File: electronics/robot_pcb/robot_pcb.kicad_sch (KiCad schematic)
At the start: 6 parts

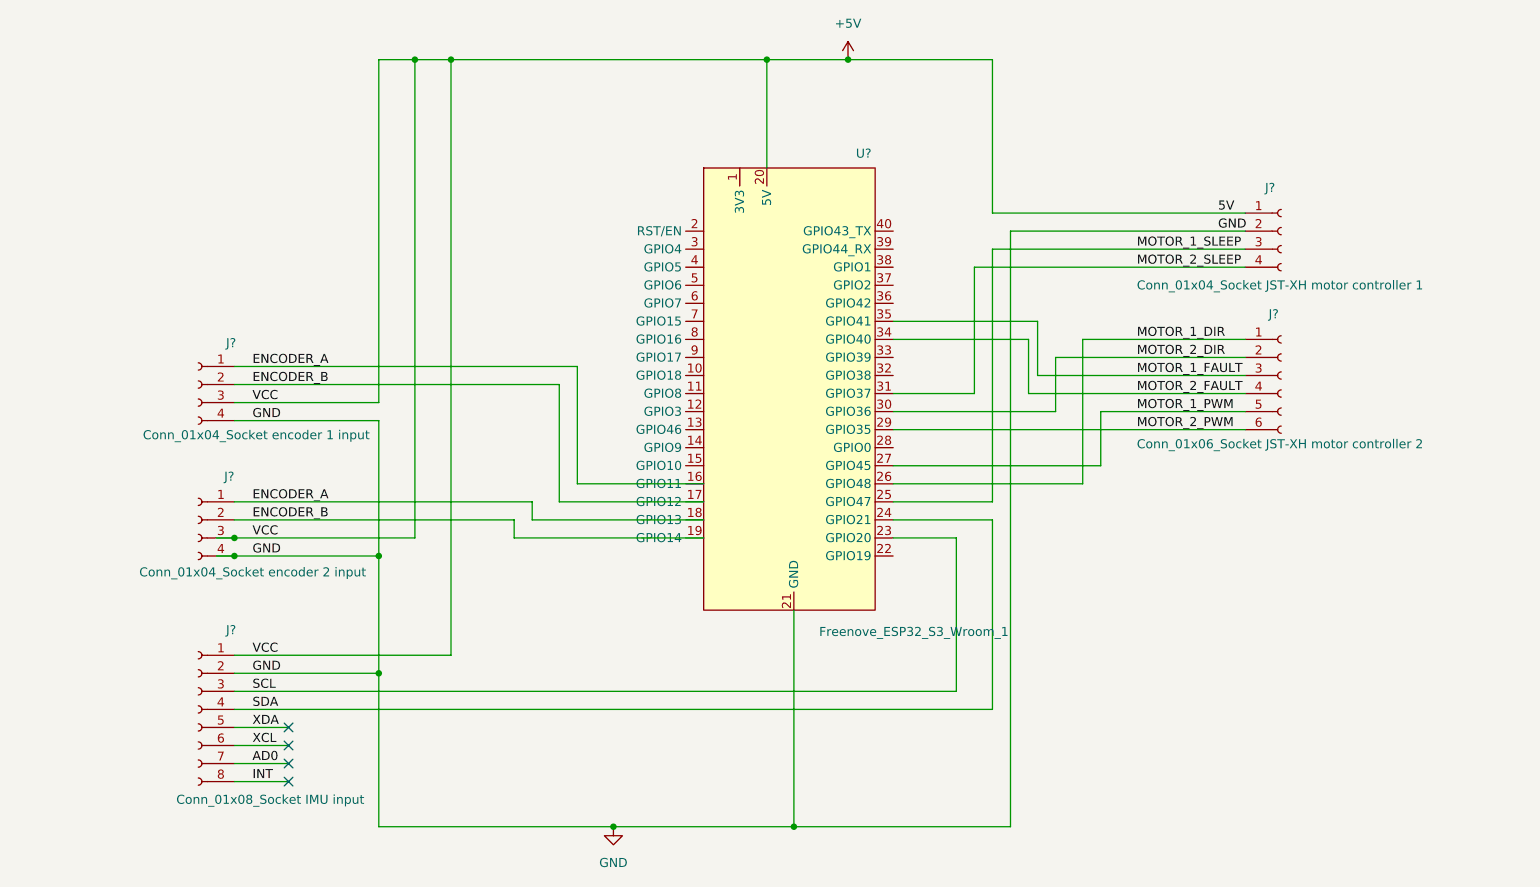
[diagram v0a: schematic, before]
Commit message: Update pin locations for easier perf board soldering
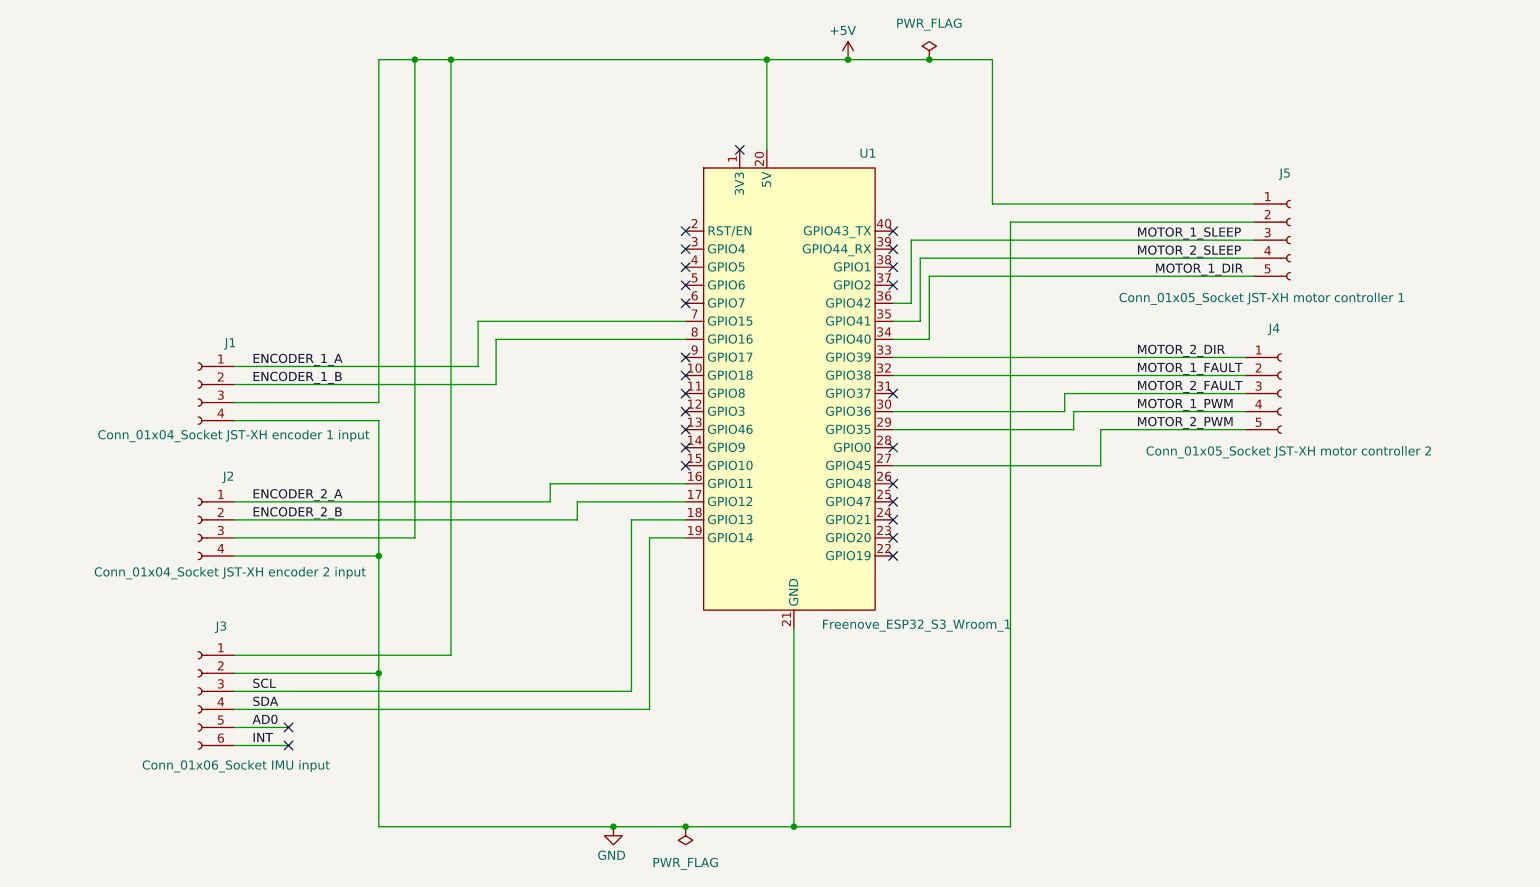
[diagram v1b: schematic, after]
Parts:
- removed J?: Conn_01x04_Socket JST-XH motor controller 1, symbol Connector:Conn_01x04_Socket
- removed J?: Conn_01x08_Socket IMU input, symbol Connector:Conn_01x08_Socket
- removed J?: Conn_01x06_Socket JST-XH motor controller 2, symbol Connector:Conn_01x06_Socket
- added J3: Conn_01x06_Socket IMU input, Connector_PinSocket_2.54mm:PinSocket_1x06_P2.54mm_Vertical, symbol Connector:Conn_01x06_Socket
- added J4: Conn_01x05_Socket JST-XH motor controller 2, Connector_PinSocket_2.54mm:PinSocket_1x05_P2.54mm_Vertical, symbol Connector:Conn_01x05_Socket
- added J5: Conn_01x05_Socket JST-XH motor controller 1, Connector_PinSocket_2.54mm:PinSocket_1x05_P2.54mm_Vertical, symbol Connector:Conn_01x05_Socket
- J1: renamed from J?; value Conn_01x04_Socket encoder 1 input -> Conn_01x04_Socket JST-XH encoder 1 input; footprint (none) -> Connector_PinSocket_2.54mm:PinSocket_1x04_P2.54mm_Vertical
- J2: renamed from J?; value Conn_01x04_Socket encoder 2 input -> Conn_01x04_Socket JST-XH encoder 2 input; footprint (none) -> Connector_PinSocket_2.54mm:PinSocket_1x04_P2.54mm_Vertical
- U1: renamed from U?; footprint (none) -> components:freenove_esp32_s3_wroom
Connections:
- net +5V: now also J3.1 (Pin_1), J5.1 (Pin_1)
- net AD0: now also J3.5 (Pin_5)
- net GND: now also J3.2 (Pin_2), J5.2 (Pin_2)
- net INT: now also J3.6 (Pin_6)
- net MOTOR_1_DIR: now also U1.34 (GPIO40), J5.5 (Pin_5); no longer U1.26 (GPIO48)
- net MOTOR_1_FAULT: now also U1.32 (GPIO38), J4.2 (Pin_2); no longer U1.35 (GPIO41)
- net MOTOR_1_PWM: now also U1.29 (GPIO35), J4.4 (Pin_4); no longer U1.27 (GPIO45)
- net MOTOR_1_SLEEP: now also U1.36 (GPIO42), J5.3 (Pin_3); no longer U1.25 (GPIO47)
- net MOTOR_2_DIR: now also U1.33 (GPIO39), J4.1 (Pin_1); no longer U1.30 (GPIO36)
- net MOTOR_2_FAULT: now also U1.30 (GPIO36), J4.3 (Pin_3); no longer U1.34 (GPIO40)
- net MOTOR_2_PWM: now also U1.27 (GPIO45), J4.5 (Pin_5); no longer U1.29 (GPIO35)
- net MOTOR_2_SLEEP: now also U1.35 (GPIO41), J5.4 (Pin_4); no longer U1.31 (GPIO37)
- net SCL: now also U1.18 (GPIO13), J3.3 (Pin_3); no longer U1.23 (GPIO20)
- net SDA: now also U1.19 (GPIO14), J3.4 (Pin_4); no longer U1.24 (GPIO21)
- net ENCODER_1_A: now reaches U1.7 (GPIO15)
- net ENCODER_1_A: now also J1.1 (Pin_1)
- net ENCODER_1_B: now reaches U1.8 (GPIO16)
- net ENCODER_1_B: now also J1.2 (Pin_2)
- net ENCODER_A renamed ENCODER_2_A
- net ENCODER_2_A: no longer J1.1 (Pin_1), U1.18 (GPIO13)
- net ENCODER_B renamed ENCODER_2_B
- net ENCODER_2_B: no longer J1.2 (Pin_2), U1.19 (GPIO14)
- no-connect marks 4 -> 26
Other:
- moved on the sheet: U1
